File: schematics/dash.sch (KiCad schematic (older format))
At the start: 31 parts, among them J1 BATT_CONN, J2 EXTERNAL_TRIGGER, J3 USB_OTG, J4 Conn_01x08, J5 Conn_01x08, SW1 SW_Push, U1 ESP-12E, U2 ch340g, U3 MCP73833, U4 HT7333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

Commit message: [add] Link to cheap components
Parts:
- U1: Link (none) -> https://fr.aliexpress.com/item/2015-New-version-1PCS-ESP-12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
- U2: Link (none) -> https://www.ebay.com/itm/5pcs-Original-CH340G-IC-R3-Board-F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
- U3: Link (none) -> https://fr.aliexpress.com/item/FREE-SHIPPING-MCP73833-FCI-U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; Sample (none) -> http://www.microchip.com/samples/Default.aspx?DeviceFamily=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
- U4: Link (none) -> https://www.ebay.com/itm/20-PCS-HT7333-HT7333-A-3-3V-SOT-89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
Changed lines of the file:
@@
 F 2 "SMD_Packages:SO-16-N" H 3950 1650 60  0001 C CNN
 F 3 "https://cdn.sparkfun.com/datasheets/Dev/Arduino/Other/CH340DS1.PDF" H 3950 1650 60  0001 C CNN
+F 4 "https://www.ebay.com/itm/5pcs-Original-CH340G-IC-R3-Board-Free-USB-Cable-Serial-chip-SOP-16-/142020477101?hash=item21111480ad:g:tHIAAOSwAKxWVtFq" H 4150 1650 60  0001 C CNN "Link"
 	1    4150 1650
 	1    0    0    -1
@@
 F 2 "sop:MSOP10" H 6950 2150 60  0001 C CNN
 F 3 "http://ww1.microchip.com/downloads/en/DeviceDoc/22005b.pdf" H 6950 2150 60  0001 C CNN
+F 4 "https://fr.aliexpress.com/item/FREE-SHIPPING-MCP73833-FCI-UN-MCP73833-73833-SOP8-20PCS/32761709020.html?ws_ab_test=searchweb0_0,searchweb201602_1_10152_10065_10151_10068_10344_10345_10342_10343_10340_10341_10540_10304_10307_10060_10302_10155_10154_10056_10055_10539_10054_10538_10537_10059_10536_10534_10533_100031_10099_10103_10102_10052_10053_10142_10107_10050_10051_10084_10083_10080_10082_10081_10177_10110_10111_10112_10113_10114_10312_10313_10314_10078_10079_10073-10112,searchweb201603_2,ppcSwitch_7&btsid=efac4eec-b878-429c-95c6-f414cb33a9ab&algo_expid=f015bd25-a6c8-4f36-b5b6-3646be386569-12&algo_pvid=f015bd25-a6c8-4f36-b5b6-3646be386569" H 6950 2150 60  0001 C CNN "Link"
+F 5 "http://www.microchip.com/samples/Default.aspx?DeviceFamily=MCP73833" H 6950 2150 60  0001 C CNN "Sample"
 	1    6950 2150
 	1    0    0    -1
@@
 F 2 "sot:SOT89" H 9400 1900 60  0001 C CNN
 F 3 "http://www.angeladvance.com/HT73xx.pdf" H 9400 1900 60  0001 C CNN
+F 4 "https://www.ebay.com/itm/20-PCS-HT7333-HT7333-A-3-3V-SOT-89-Low-Power-Consumption-LDO-Voltage-Regulator-/191780758722?epid=1075406669&hash=item2ca70624c2:g:iHAAAOSwJkJWlH2L" H 9400 1900 60  0001 C CNN "Link"
 	1    9400 1900
 	1    0    0    -1
@@
 F 2 "ESP8266:ESP-12E_SMD" H 6650 4650 50  0001 C CNN
 F 3 "https://www.elecrow.com/download/ESP-12F.pdf" H 6650 4650 50  0001 C CNN
+F 4 "https://fr.aliexpress.com/item/2015-New-version-1PCS-ESP-12F-ESP-12E-upgrade-ESP8266-remote-serial-Port-WIFI-wireless-module/32649968409.html?ws_ab_test=searchweb0_0,searchweb201602_1_10152_10065_10151_10068_10344_10345_10342_10343_10340_10341_10540_10304_10307_10060_10302_10155_10154_10056_10055_10539_10054_10538_10537_10059_10536_10534_10533_100031_10099_10103_10102_10052_10053_10142_10107_10050_10051_10084_10083_10080_10082_10081_10177_10110_10111_10112_10113_10114_10312_10313_10314_10078_10079_10073-10110,searchweb201603_2,ppcSwitch_7&btsid=373d46ce-cda7-4a8b-b90d-3cadb2de28fd&algo_expid=d60f9745-2e5e-4a03-b5a4-ab069689f003-1&algo_pvid=d60f9745-2e5e-4a03-b5a4-ab069689f003" H 6650 4650 60  0001 C CNN "Link"
 	1    6650 4650
 	1    0    0    -1

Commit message: [add] Link to ebay
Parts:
- J1: Link (none) -> https://www.ebay.com/itm/50-sets-Micro-JST-SH-1-0mm-2-Pin-F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
- J2, J4, J5: Link (none) -> https://www.ebay.com/itm/10pcs-2-54MM-1-40Pin-SMD-SMT-1-40P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
- J3: Link (none) -> https://www.ebay.com/itm/20pcs-Micro-USB-Type-B-Female-Sock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
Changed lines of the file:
@@
 F 2 "Connectors_JST:JST_SH_SM02B-SRSS-TB_02x1.00mm_Angled" H 8450 2150 50  0001 C CNN
 F 3 "" H 8450 2150 50  0001 C CNN
+F 4 "https://www.ebay.com/itm/50-sets-Micro-JST-SH-1-0mm-2-Pin-Female-Connector-with-Wire-and-Male-Connector/172166255853?hash=item2815e894ed:g:rGcAAOSwaZdXHwHf" H 8450 2150 60  0001 C CNN "Link"
 	1    8450 2150
 	-1   0    0    1
@@
 F 2 "Pin_Headers:Pin_Header_Straight_1x02_Pitch2.54mm_SMD_Pin1Left" H 4950 3750 50  0001 C CNN
 F 3 "" H 4950 3750 50  0001 C CNN
+F 4 "https://www.ebay.com/itm/10pcs-2-54MM-1-40Pin-SMD-SMT-1-40Pin-Male-Single-Row-Pin-Header/261879748701?ssPageName=STRK%3AMEBIDX%3AIT&_trksid=p2060353.m2749.l2649" H 4950 3750 60  0001 C CNN "Link"
 	1    4950 3750
 	0    -1   -1   0
@@
 F 2 "Connectors_USB:USB_Micro-B_Molex_47346-0001" H 1450 1900 50  0001 C CNN
 F 3 "" H 1450 1900 50  0001 C CNN
+F 4 "https://www.ebay.com/itm/20pcs-Micro-USB-Type-B-Female-Socket-5-Pin-Connector-SMD-Soldering-BB/311979527669?epid=2265640141&hash=item48a36dcdf5:g:63EAAOSwB3tZpAxU" H 1300 1950 60  0001 C CNN "Link"
 	1    1300 1950
 	1    0    0    -1
@@
 F 2 "Pin_Headers:Pin_Header_Straight_1x08_Pitch2.54mm" H 3350 5650 50  0001 C CNN
 F 3 "" H 3350 5650 50  0001 C CNN
+F 4 "https://www.ebay.com/itm/10pcs-2-54MM-1-40Pin-SMD-SMT-1-40Pin-Male-Single-Row-Pin-Header/261879748701?hash=item3cf93fd85d:g:XAAAAOSwPhdVSx-I" H 3350 5650 60  0001 C CNN "Link"
 	1    3350 5650
 	0    1    1    0
@@
 F 2 "Pin_Headers:Pin_Header_Straight_1x08_Pitch2.54mm" H 2100 5650 50  0001 C CNN
 F 3 "" H 2100 5650 50  0001 C CNN
+F 4 "https://www.ebay.com/itm/10pcs-2-54MM-1-40Pin-SMD-SMT-1-40Pin-Male-Single-Row-Pin-Header/261879748701?hash=item3cf93fd85d:g:XAAAAOSwPhdVSx-I" H 2100 5650 60  0001 C CNN "Link"
 	1    2100 5650
 	0    1    1    0

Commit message: [add] Link to buy switch on ebay
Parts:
- SW1: Link (none) -> https://www.ebay.com/itm/100pcs-3-6-2-5mm-Tactile-Push-Butt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
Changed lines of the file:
@@
 F 2 "Buttons_Switches_SMD:SW_DIP_x1_W5.08mm_Slide_Copal_CHS-A" H 4950 4550 50  0001 C CNN
 F 3 "" H 4950 4550 50  0001 C CNN
+F 4 "https://www.ebay.com/itm/100pcs-3-6-2-5mm-Tactile-Push-Button-Switch-Tact-Switch-Micro-Switch-2-Pin-SMD/400985332185?ssPageName=STRK%3AMEBIDX%3AIT&_trksid=p2057872.m2749.l2649" V 4950 4350 60  0001 C CNN "Link"
 	1    4950 4350
 	1    0    0    -1

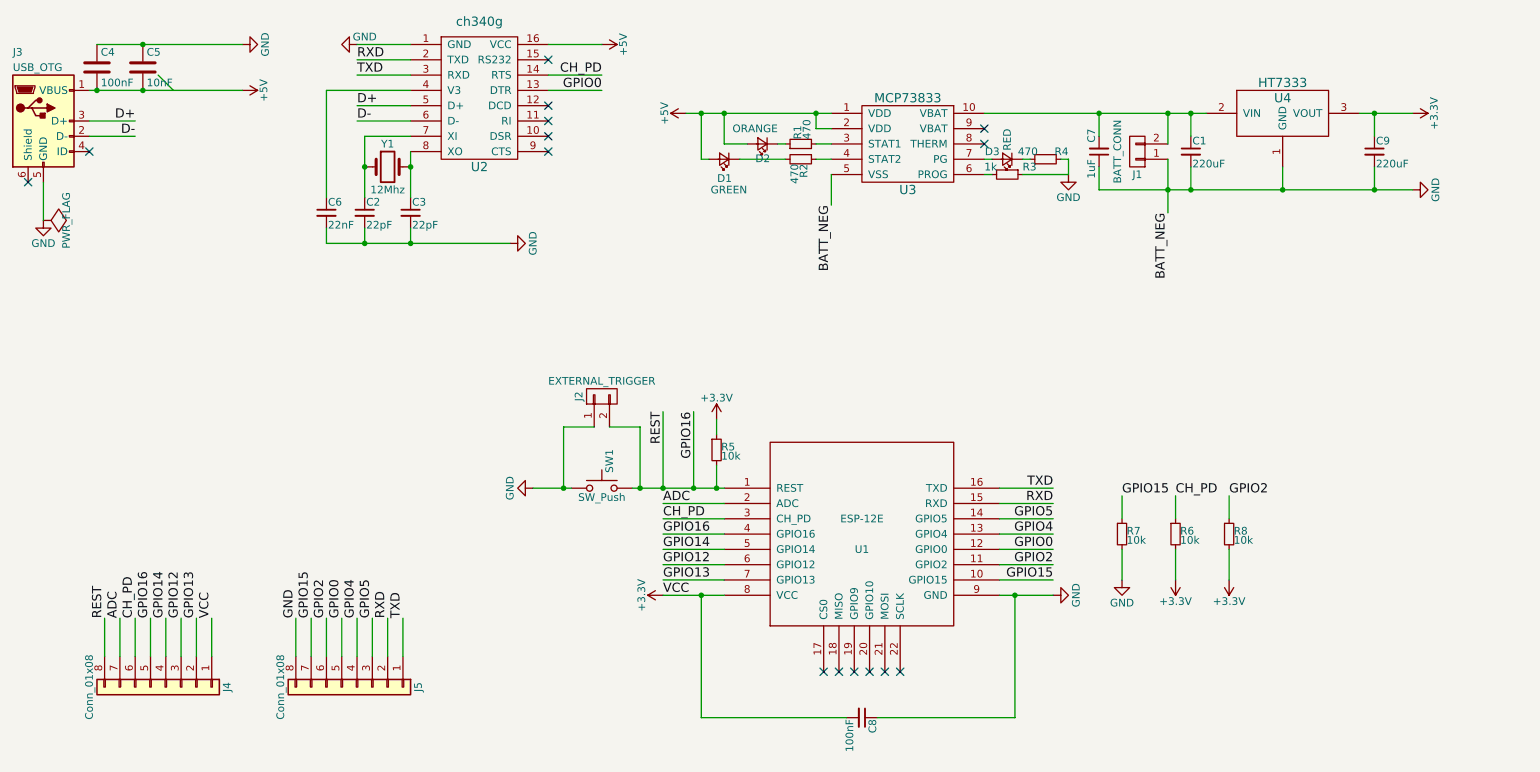
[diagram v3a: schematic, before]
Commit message: [chg] License to a hardware license
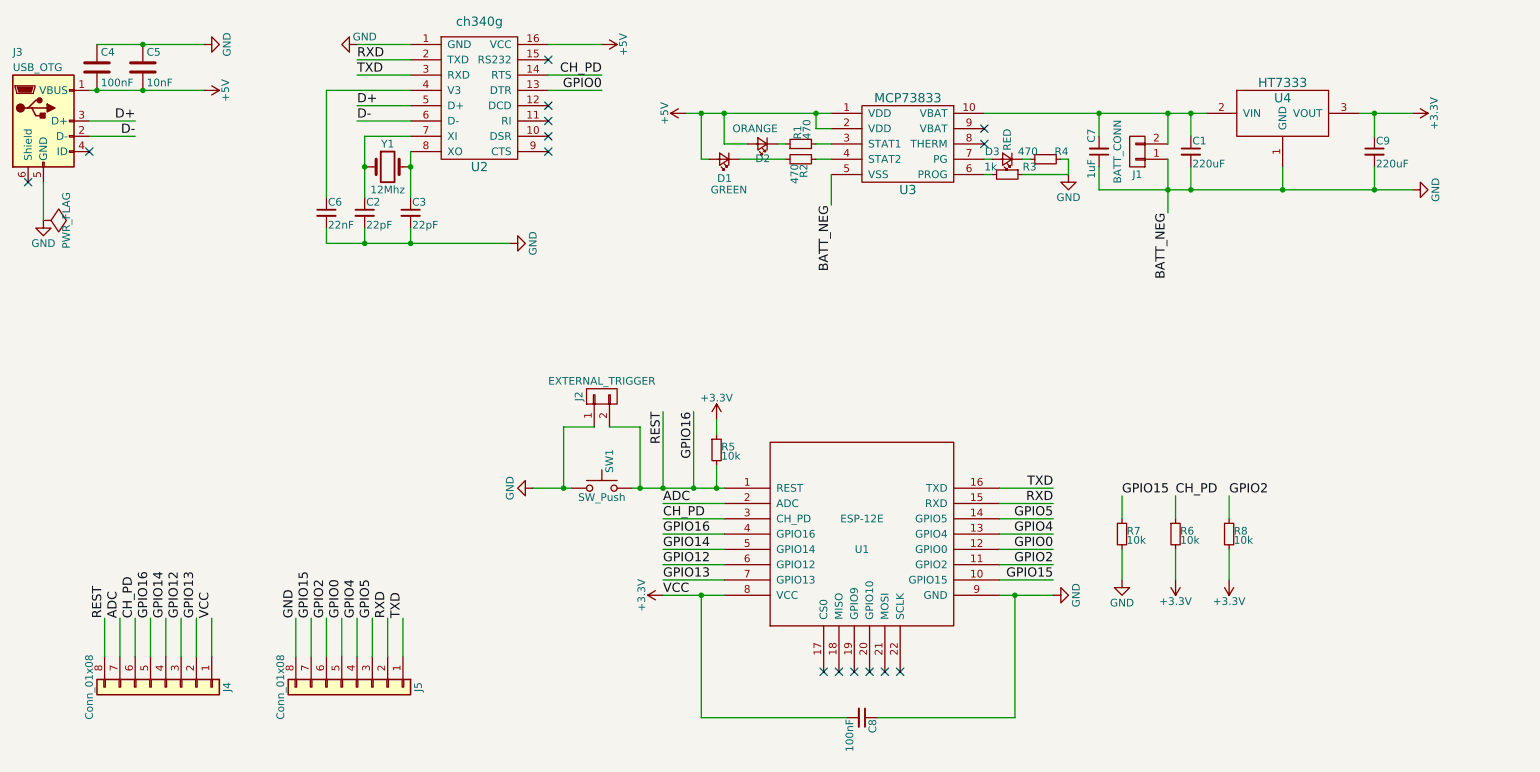
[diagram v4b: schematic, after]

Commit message: [fix] Change footprints to match component buyed
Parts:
- SW1: footprint Buttons_Switches_SMD:SW_DIP_x1_W5.08mm_Slide_Copal_CHS-A -> KiCad/Buttons_Switches_SMD.pretty:SW_DIP_x1_W5.9mm_Slide_Copal_CVS
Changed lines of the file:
@@
 F 0 "SW1" V 5000 4450 50  0000 L CNN
 F 1 "SW_Push" H 4950 4290 50  0000 C CNN
-F 2 "Buttons_Switches_SMD:SW_DIP_x1_W5.08mm_Slide_Copal_CHS-A" H 4950 4550 50  0001 C CNN
+F 2 "KiCad/Buttons_Switches_SMD.pretty:SW_DIP_x1_W5.9mm_Slide_Copal_CVS" H 4950 4550 50  0001 C CNN
 F 3 "" H 4950 4550 50  0001 C CNN
 F 4 "https://www.ebay.com/itm/100pcs-3-6-2-5mm-Tactile-Push-Button-Switch-Tact-Switch-Micro-Switch-2-Pin-SMD/400985332185?ssPageName=STRK%3AMEBIDX%3AIT&_trksid=p2057872.m2749.l2649" V 4950 4350 60  0001 C CNN "Link"

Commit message: load sharing (USB <-> battery), change to MCP73831
add all lib dependencies locally
restructure dirs
less vias in pads !
change top copper pour to 5V, not 3,3V

type fottprint in readme
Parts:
- removed D2: ORANGE, LEDs:LED_1206, symbol LED_Small
- removed D3: RED, LEDs:LED_1206, symbol LED_Small
- removed R1, R4: 470, Resistors_SMD:R_1206_HandSoldering, symbol R_Small
- removed U3: MCP73833, sop:MSOP10, symbol MCP73833
- added D4: D_Schottky, sot:SOT23, symbol D_Schottky
- added Q1: MOSFET_PCH, Silicon-Standard:SOT23-3, symbol MOSFET_PCH-IRLML2244
- added R9: 100k, Resistors_SMD:R_1206_HandSoldering, symbol R_Small
- added U3: MCP73831, sot:SOT23-5, symbol MCP73831
- R3: value 1k -> 10k
- U4: symbol HT73xx -> HT73xx-RESCUE-dash
- Y1: footprint Crystals:Crystal_SMD_3225-4pin_3.2x2.5mm_HandSoldering -> Crystals:Crystal_SMD_5032_4Pads
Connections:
- net +5V: now also D4.2 (A), Q1.1 (G), R9.1, U3.4 (VIN)
- net GND: now also R9.2, U3.2 (VSS)
- net at C7.2, J1.2 (P2): now also Q1.3 (D), U3.3 (VBAT); no longer C1.1, U4.2 (VIN)
- net XI: now reaches C2.1, U2.7 (XI), Y1.1
- net XO: now reaches C3.1, U2.8 (XO), Y1.2
- net at R2.1: now also U3.1 (STAT)
- net at R3.2: now also U3.5 (PROG)
- new net: C1.1, D4.1 (K), Q1.2 (S), U4.2 (VIN)
- no-connect marks 15 -> 13
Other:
- moved on the sheet: C1, C7, C9, D1, J1, R2, R3, U4

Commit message: finish routing
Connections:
- net GND: now also J3.6 (Shield)
- no-connect marks 13 -> 12
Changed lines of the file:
@@
 $EndComp
 NoConn ~ 1600 2150
-NoConn ~ 1200 2350
 Text Label 7900 4350 2    60   ~ 0
 TXD
@@
 Text Label 3700 2350 0    60   ~ 0
 XO
+Wire Wire Line
+	1200 2350 1200 2400
+Wire Wire Line
+	1200 2400 1300 2400
+Connection ~ 1300 2400
 $EndSCHEMATC
